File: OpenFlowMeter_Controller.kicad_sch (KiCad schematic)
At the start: 43 parts, among them J3 Conn_01x06, J5 Conn_01x03, J6 Conn_02x04_Odd_Even, J7 Conn_02x03_Odd_Even, U2 STM32F103C8Tx, U5 SN65HVD231, U7 24LC64, U9 TMP100, Y1 12 MHz

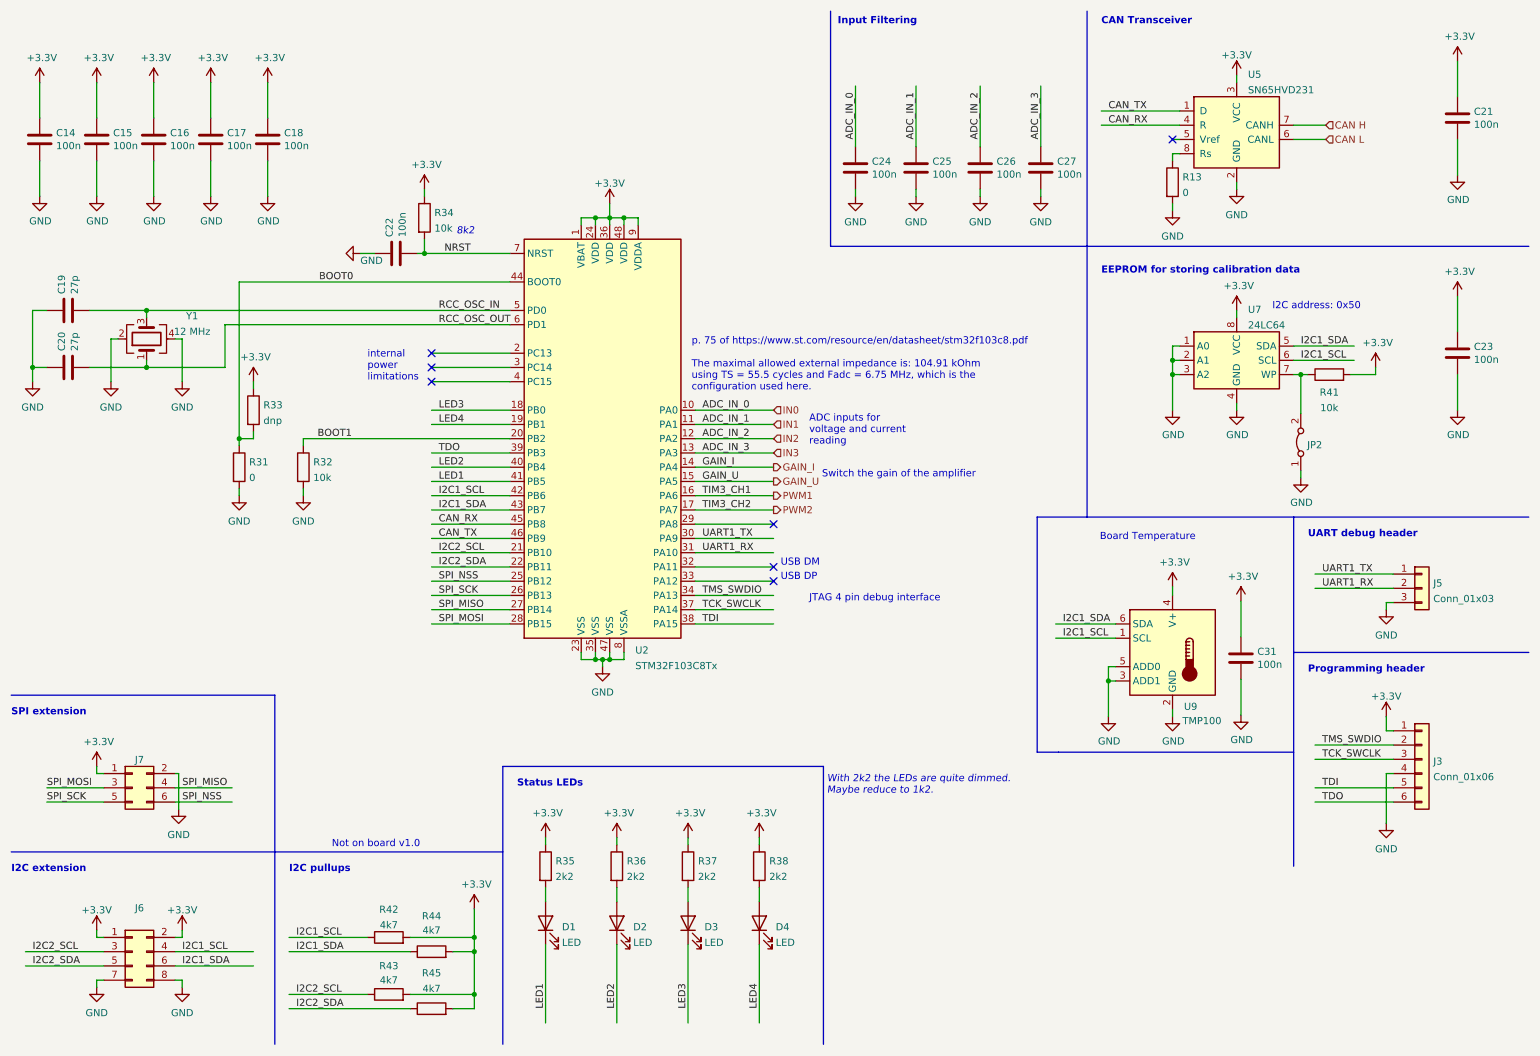
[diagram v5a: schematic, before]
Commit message: moved I2C components into subscheet
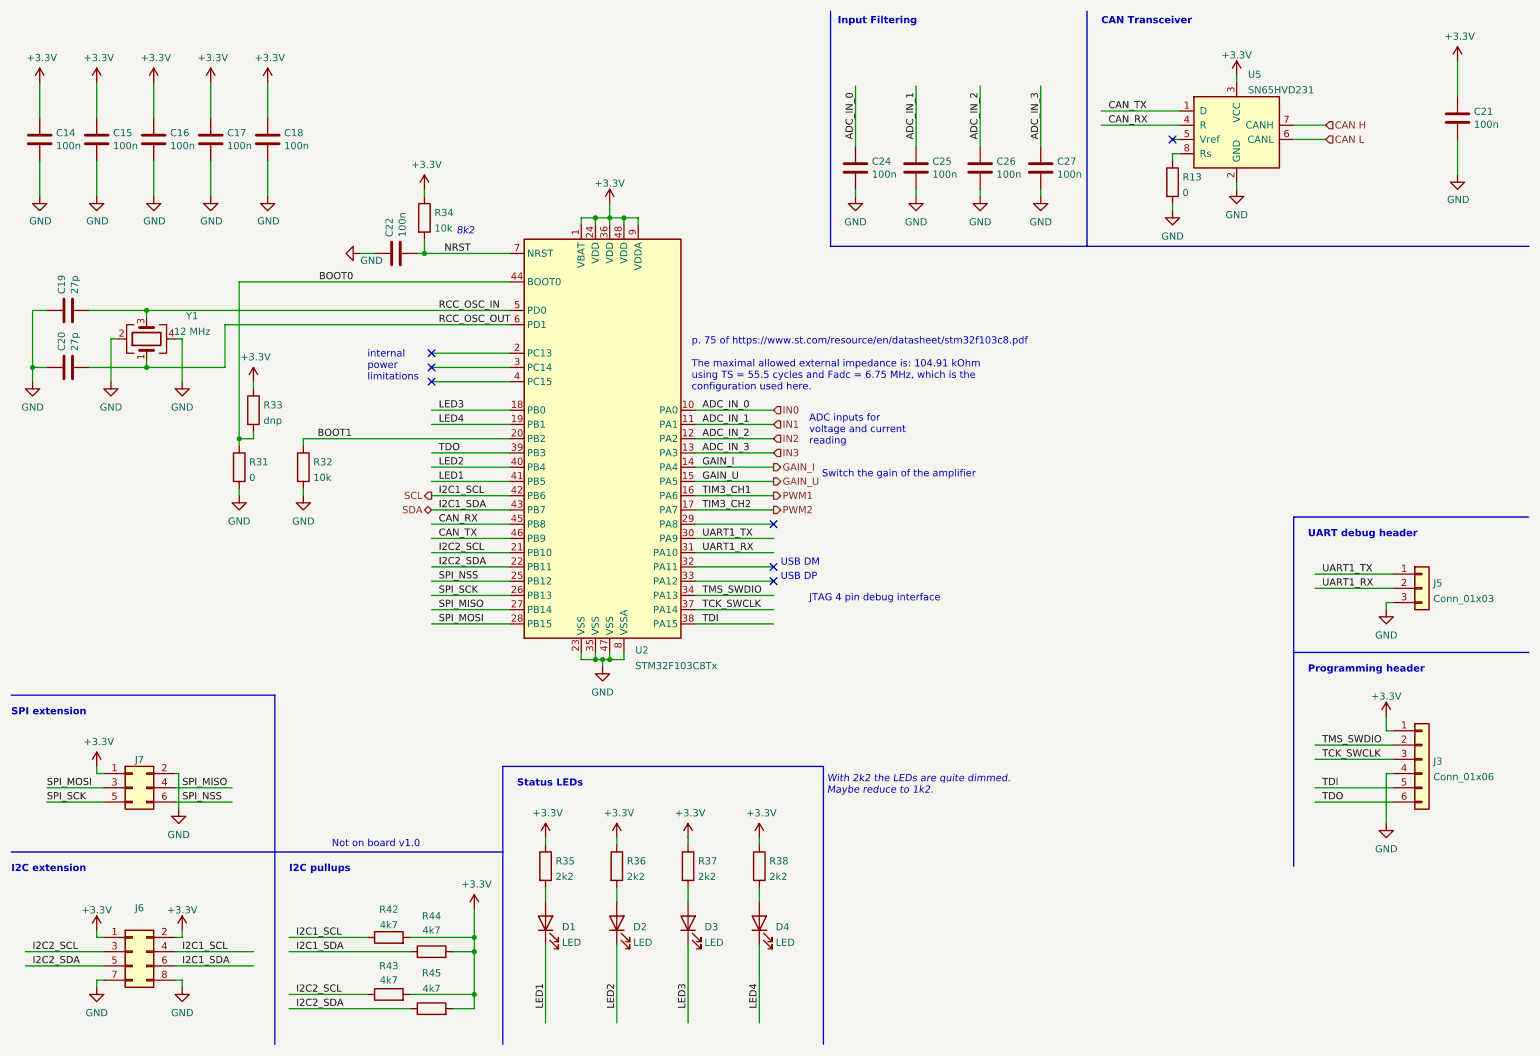
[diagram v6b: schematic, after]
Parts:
- removed C23, C31: 100n, Capacitor_SMD:C_0603_1608Metric, symbol Device:C
- removed JP2: Jumper_2_Bridged, Jumper:SolderJumper-2_P1.3mm_Bridged_RoundedPad1.0x1.5mm, symbol Jumper:Jumper_2_Bridged
- removed R41: 10k, Resistor_SMD:R_0603_1608Metric, symbol Device:R
- removed U7: 24LC64, Package_DIP:DIP-8_W7.62mm, symbol Memory_EEPROM:24LC64
- removed U9: TMP100, Package_TO_SOT_SMD:SOT-23-6, symbol Sensor_Temperature:TMP100
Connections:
- net I2C1_SCL renamed SCL
- net I2C1_SDA renamed SDA
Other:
- note removed: "Board Temperature"
- note removed: "EEPROM for storing calibration data"
- note removed: "I2C address: 0x50"

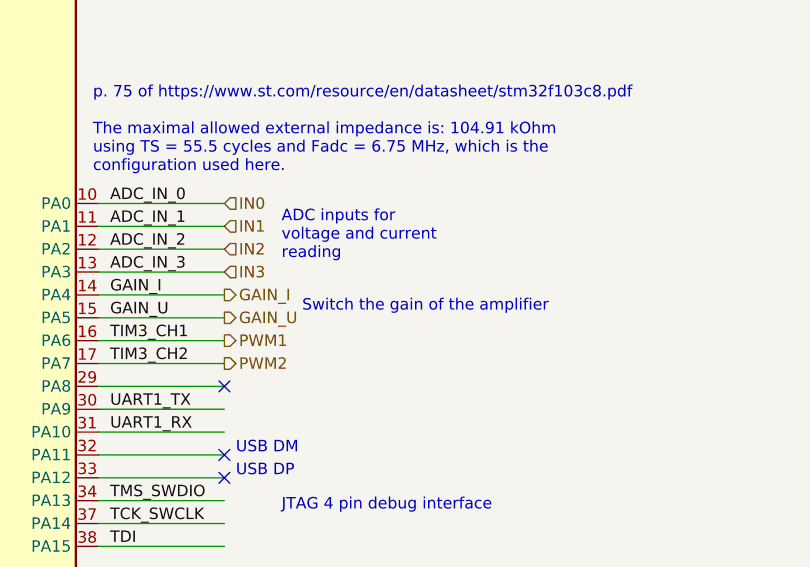
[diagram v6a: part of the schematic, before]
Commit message: added some lines to structure the STM32 ports
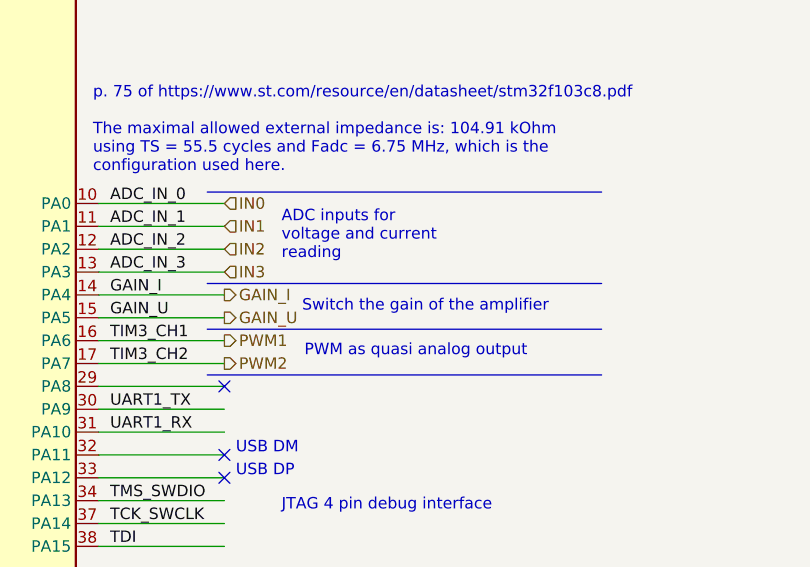
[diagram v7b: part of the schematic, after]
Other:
- note added: "PWM as quasi analog output"
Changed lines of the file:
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@@
+    (stroke (width 0) (type default) (color 0 0 0 0))
+  )
+  (polyline (pts (xy 147.955 82.55) (xy 191.77 82.55))
     (stroke (width 0) (type default) (color 0 0 0 0))
   )
@@
     (stroke (width 0) (type default) (color 0 0 0 0))
   )
+  (polyline (pts (xy 147.955 102.87) (xy 191.77 102.87))
+    (stroke (width 0) (type default) (color 0 0 0 0))
+  )
   (wire (pts (xy 118.11 49.53) (xy 115.57 49.53))
     (stroke (width 0) (type default) (color 0 0 0 0))
@@
     (stroke (width 0) (type default) (color 0 0 0 0))
   )
+  (polyline (pts (xy 147.955 97.79) (xy 191.77 97.79))
+    (stroke (width 0) (type default) (color 0 0 0 0))
+  )
   (wire (pts (xy 33.02 71.12) (xy 31.75 71.12))
     (stroke (width 0) (type default) (color 0 0 0 0))
@@
   )
   (wire (pts (xy 54.61 60.96) (xy 102.87 60.96))
+    (stroke (width 0) (type default) (color 0 0 0 0))
+  )
+  (polyline (pts (xy 147.955 92.71) (xy 191.77 92.71))
     (stroke (width 0) (type default) (color 0 0 0 0))
   )
@@
     (effects (font (size 1.27 1.27)) (justify left bottom))
   )
+  (text "PWM as quasi analog output" (at 158.75 100.965 0)
+    (effects (font (size 1.27 1.27)) (justify left bottom))
+  )
